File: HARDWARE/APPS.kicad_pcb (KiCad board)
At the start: 2 copper layers, 100 x 75 mm, 95 parts, among them J4 Sygnały, J5 Diagnostyka, J8 Zasilanie+CAN, K1 FINDER-30.22, Q1 BSS138, SW1 SW_Push, U1 STM32L4P5RET6, U10 MCP6001, U2 MCP6001, U3 LM1117-3.3, U4 LM1117-3.3, U5 LM1117-3.3, U6 MCP2562-H-SN, U7 MCP6N11-005, U9 MCP6N11-005, Y1 Crystal_GND24

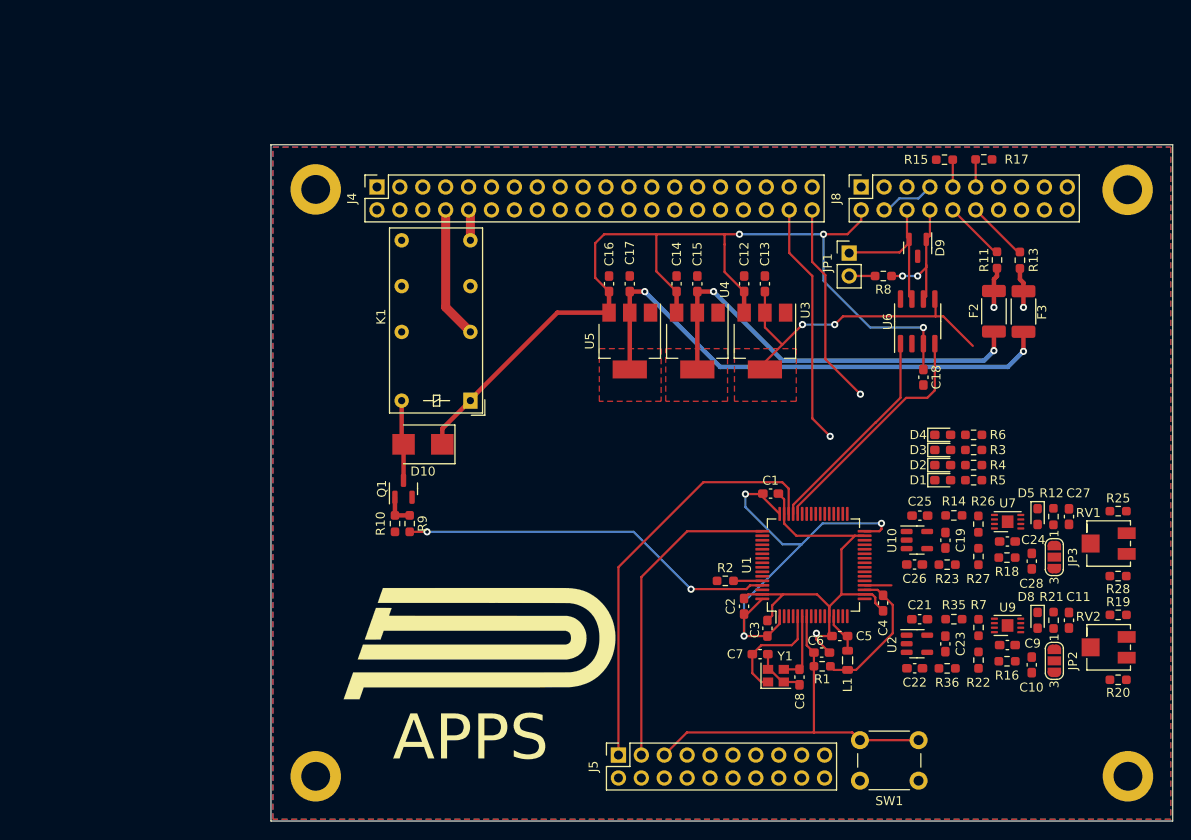
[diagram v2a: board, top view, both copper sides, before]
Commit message: Route PCB tracks
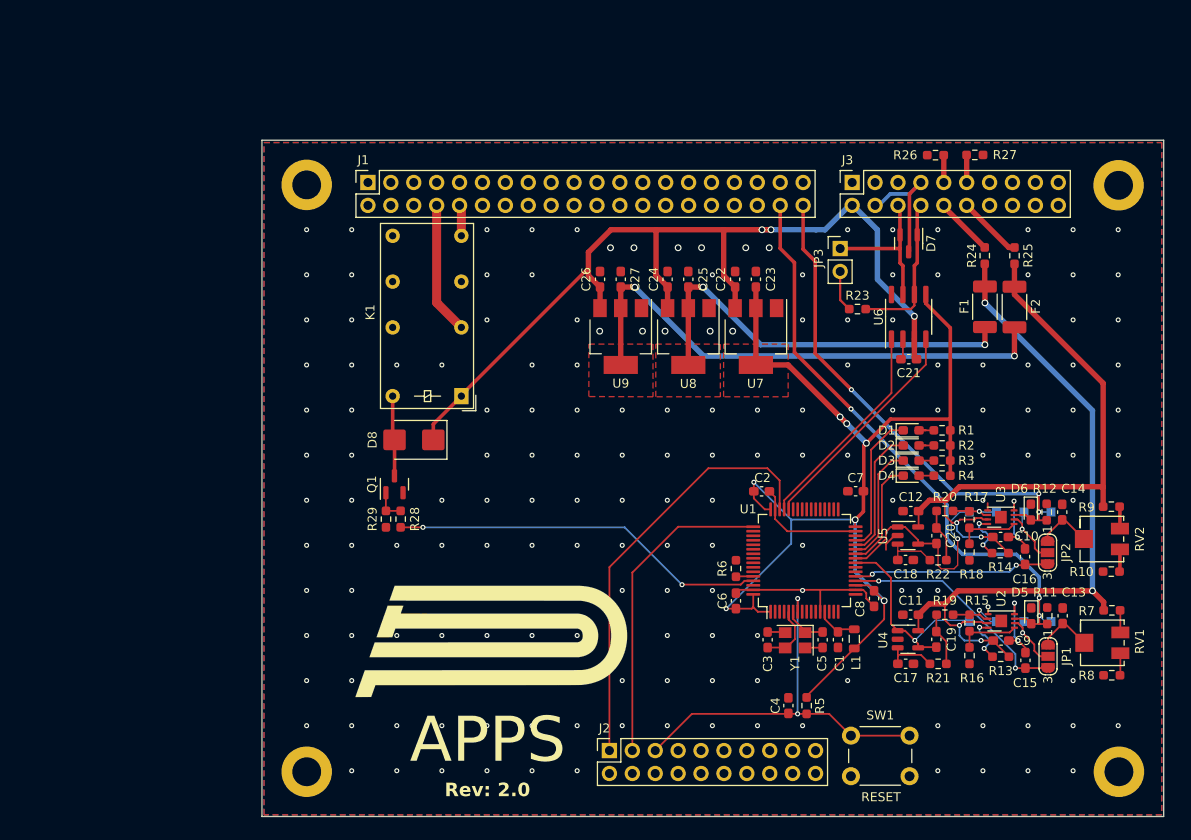
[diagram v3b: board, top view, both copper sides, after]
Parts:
- removed the C6 at (161.1, 122.9)
- removed the C8 at (158.7, 125.6)
- removed the G*** at (148.6, 97.1)
- removed the R1 at (161.2, 124.4)
- added C1: 100n, Capacitor_SMD:C_0603_1608Metric_Pad1.08x0.95mm_HandSolder, F.Cu at (162.9, 121.5)
- added C4: 100n, Capacitor_SMD:C_0603_1608Metric_Pad1.08x0.95mm_HandSolder, F.Cu at (157.4, 128.8)
- added R5: 10k, Resistor_SMD:R_0603_1608Metric_Pad0.98x0.95mm_HandSolder, F.Cu at (159.4, 128.8)
- added TP1: P1, TestPoint:TestPoint_Pad_1.0x1.0mm, B.Cu at (186.6, 119.5)
- added TP2: N1, TestPoint:TestPoint_Pad_1.0x1.0mm, B.Cu at (183.6, 119.5)
- added TP3: O1, TestPoint:TestPoint_Pad_1.0x1.0mm, B.Cu at (180.5, 119.5)
- added TP4: F1, TestPoint:TestPoint_Pad_1.0x1.0mm, B.Cu at (177.5, 119.5)
- added TP5: P2, TestPoint:TestPoint_Pad_1.0x1.0mm, B.Cu at (186.6, 107.3)
- added TP6: N2, TestPoint:TestPoint_Pad_1.0x1.0mm, B.Cu at (183.6, 107.3)
- added TP7: O2, TestPoint:TestPoint_Pad_1.0x1.0mm, B.Cu at (180.5, 107.3)
- added TP8: F2, TestPoint:TestPoint_Pad_1.0x1.0mm, B.Cu at (177.5, 107.3)
- C2: renamed from C1; value 100nF -> 100n
- C21: renamed from C18; value 100nF -> 100n
- C22: renamed from C12; value 100nF -> 100n
- C23: renamed from C13; value 100nF -> 100n
- C24: renamed from C14; value 100nF -> 100n
- C25: renamed from C15; value 100nF -> 100n
- C26: renamed from C16; value 100nF -> 100n
- C27: renamed from C17; value 100nF -> 100n
- C3, C5: value 100nF -> 22p
- C6: renamed from C2; value 100nF -> 100n
- C7: value 22pF -> 100n
- C8: renamed from C4; value 100nF -> 100n
- J1: renamed from J4; value Sygnały -> Signals
- J2: renamed from J5; value Diagnostyka -> Diagnostics
- J3: renamed from J8; value Zasilanie+CAN -> Power & CAN
- JP3: renamed from JP1; value Jumper_NC_Small -> Terminator
- Y1: value Crystal_GND24 -> 8Mhz; footprint Crystal:Crystal_SMD_2520-4Pin_2.5x2.0mm -> Crystal:Crystal_SMD_3225-4Pin_3.2x2.5mm
- moved C7 20.9 mm to (164.9, 105.0), turned to 180 degrees
- moved G*** 10.6 mm to (149.2, 103.4)
- moved R23 4.66 mm to (165.1, 84.8)
- moved Y1 4.47 mm to (158.2, 121.5), turned to 180 degrees
- moved D1 3.54 mm to (171.0, 98.2)
- moved D2 3.54 mm to (171.0, 99.9)
- moved D3 3.54 mm to (171.0, 101.6)
- moved D4 3.54 mm to (171.0, 103.3)
- moved R1 3.54 mm to (174.5, 98.2)
- moved R2 3.54 mm to (174.5, 99.9)
- moved R3 3.54 mm to (174.5, 101.6)
- moved R4 3.54 mm to (174.5, 103.3)
- moved C21 2.58 mm to (170.8, 90.4), turned to 180 degrees
- moved L1 2.50 mm to (164.7, 121.4)
- moved C5 1.95 mm to (161.2, 121.5), turned to -90 degrees
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- renumbered C24 to C10, C21 to C11, C25 to C12, C11 to C13, C27 to C14, C10 to C15, C28 to C16, C22 to C17, C26 to C18, C23 to C19, C19 to C20, D4 to D1, D3 to D2, D2 to D3, D1 to D4, D8 to D5, D5 to D6, D9 to D7, D10 to D8, F2 to F1, F3 to F2, JP2 to JP1, JP3 to JP2, R6 to R1, R28 to R10, R21 to R11, R16 to R13, R18 to R14, R7 to R15, R22 to R16, R26 to R17, R27 to R18, R35 to R19, R3 to R2, R14 to R20, R36 to R21, R23 to R22, R8 to R23, R11 to R24, R13 to R25, R15 to R26, R17 to R27, R9 to R28, R10 to R29, R4 to R3, R5 to R4, R2 to R6, R19 to R7, R20 to R8, R25 to R9, RV2 to RV1, RV1 to RV2, U9 to U2, U7 to U3, U2 to U4, U10 to U5, U3 to U7, U4 to U8, U5 to U9
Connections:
- C3 pad 1: /3V3_SYS -> /XTAL1
- C5 pad 1: /3V3_A -> /XTAL2
- C7 pad 1: /XTAL1 -> /3V3_SYS
- Y1 pad 1: /XTAL1 -> /XTAL2
- Y1 pad 3: /XTAL2 -> /XTAL1
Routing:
- net 3V3_POT1: track 4.44 -> 80.7 mm, vias 1 -> 4
- net 3V3_POT2: track 4.47 -> 69.5 mm, vias 1 -> 2
- net SIG_APPS1: track 27.0 -> 67.3 mm, vias 1 -> 3
- net SIG_APPS2: track 22.7 -> 56.4 mm, vias 1 -> 3
- net /3V3_SYS: track 101.9 -> 132.9 mm, vias 5 -> 7
- net /SENSOR2: track 0.00 -> 24.6 mm, vias 0 -> 1
- net /DAC_REF1: track 2.98 -> 26.3 mm, vias 0 -> 2
- net /SENSOR1: track 0.00 -> 23.2 mm, vias 0 -> 1
- net /DAC_REF2: track 0.00 -> 21.8 mm, vias 0 -> 2
- net /LED4: track 0.00 -> 15.8 mm
- net /LED3: track 0.00 -> 14.6 mm
- net /LED2: track 0.00 -> 13.4 mm
- net /LED1: track 0.00 -> 12.3 mm
- net GND: track 62.3 -> 72.4 mm, vias 1 -> 178
- net Net-(JP2-C): track 0.00 -> 7.99 mm, vias 0 -> 1
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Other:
- board text added: "RESET"
- board text added: "Rev: 2.0"
